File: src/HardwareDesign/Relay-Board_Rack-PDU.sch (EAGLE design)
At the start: 16 parts

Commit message: add SMPS to relay board
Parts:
- added BR1: DBLS207G, rectifier:DBLS207G
- added C14: 100nF 275V, ds_passive:C
- added C15, C17: 15uF 400V, Capacitor:C-POL_RADIAL-25MM-DIA
- added C16: 10nF 1kV, ds_passive:C-1206
- added C18: 470uF 25V, Capacitor:C-POL_RADIAL-11MM-DIA
- added C19, C25: 100uF 25V, Capacitor:C-POL_RADIAL-11MM-DIA
- added C20: 1uF 25V, ds_passive:C-0805
- added C21: 10nF 50V, ds_passive:C-0805
- added C22: 2.2nF 50V, ds_passive:C-0603
- added C23: 33nF 16V, ds_passive:C-0603
- added C24: 220pF, ds_passive:C-0805
- added C26: DE2E3KY222MA2BM01, ds_passive:C102-1KV
- added CM1: 20mH CM CHOKE, ds_trafo:WE-CMB_XS_744821120
- added CON1: (no value), ds_con:CON-2X7
- added D15: MRA4007T3G, Diodes:SS12
- added D16: STPS5H100B, ds_active:STPS5H100B
- added D17, D18, D19: BAT41ZFILM, diode:CGRM4001-G
- added D20: MMSZ5248B-V-GS08, Diodes-2:BZG03C240-HM3-08
- added F2: 696101000002, Wurth_Connectors_WR-FSH:696101000002
- added IC3: TS432ILT, ds_ic_vreg:TS432ILT
- added IC4: (no value), ds_ic_peripherals:VIPER35HD
- added L2: 3.3uH SD43-332ML, 52101-101-REV-A_v16:INDUCTOR-BOURNS_SRN8040
- added OPT2: SFH6106-2T, ds_ic_peripherals:SFH6106-3SMD-4_SFH610X_VIS-M
- added R13: 220K 5% 0.33W 200V, ds_passive:R1206
- added R14: 1K, ds_passive:R0603
- added R15: 12K, ds_passive:R0603
- added R16: 82K, ds_passive:R0603
- added R17: 130K 1%, ds_passive:R0603
- added R18: 15K 1%, ds_passive:R0603
- added R19: 4.7R 1%, ds_passive:R0603
- added R20: 330K 1%, ds_passive:R0603
- added R21: 133K 1%, ds_passive:R0603
- added R22: 30K 1%, ds_passive:R0603
- added R23: 47K 1%, ds_passive:R0603
- added R24: 220R, ds_passive:R0805
- added RV1: B72210S0321K101, varistor:S10K40
- added T1: 750370228, ds_trafo:750370228
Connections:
- new net AC_LINE2: C14.2, CM1.1, RV1.2
- new net AGND: BR1.-, C15.-, C17.-, C22.2, C24.2, C25.-, C26.1, D17.A, D20.A, IC4.BR, IC4.GND, OPT2.4, R22.2, R23.2, T1.3
- new net DC_RAW: BR1.+, C15.+, C16.1, C17.+, R13.2, T1.6
- new net FB: C22.1, C23.1, IC4.FB, OPT2.3
- new net GND: C18.-, C19.-, C20.2, C26.2, IC3.3, R18.2, T1.10
- new net N$12: BR1.AC2, CM1.3
- new net N$20: C14.1, CM1.2, F2.2, RV1.1
- new net N$22: C16.2, D15.C, R13.1
- new net N$23: D15.A, IC4.DRAIN, T1.4
- new net N$24: D16.2, T1.8
- new net N$25: C18.+, D16.3, L2.1, R14.1
- new net N$26: IC3.2, OPT2.1, R14.2, R15.1
- new net N$27: OPT2.2, R15.2, R16.1
- new net N$28: C21.1, R16.2
- new net N$29: C21.2, IC3.1, R17.2, R18.1
- new net N$30: C24.1, C25.+, D19.C, IC4.VDD, R24.1
- new net N$31: D19.A, R19.2
- new net N$32: D18.A, R19.1, R20.1, T1.1
- new net N$33: D17.C, D18.C, R21.1
- new net N$34: IC4.ZCD, R20.2, R21.2, R22.1
- new net N$35: C23.2, R23.1
- new net N$36: D20.C, R24.2
- new net N$5: BR1.AC1, CM1.4
- net +12V: now also C19.+, C20.1, L2.2, R17.1
- net AC_LINE: now also F2.1
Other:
- note added: "12 V - 15 W FLYBACK CONVERTER"

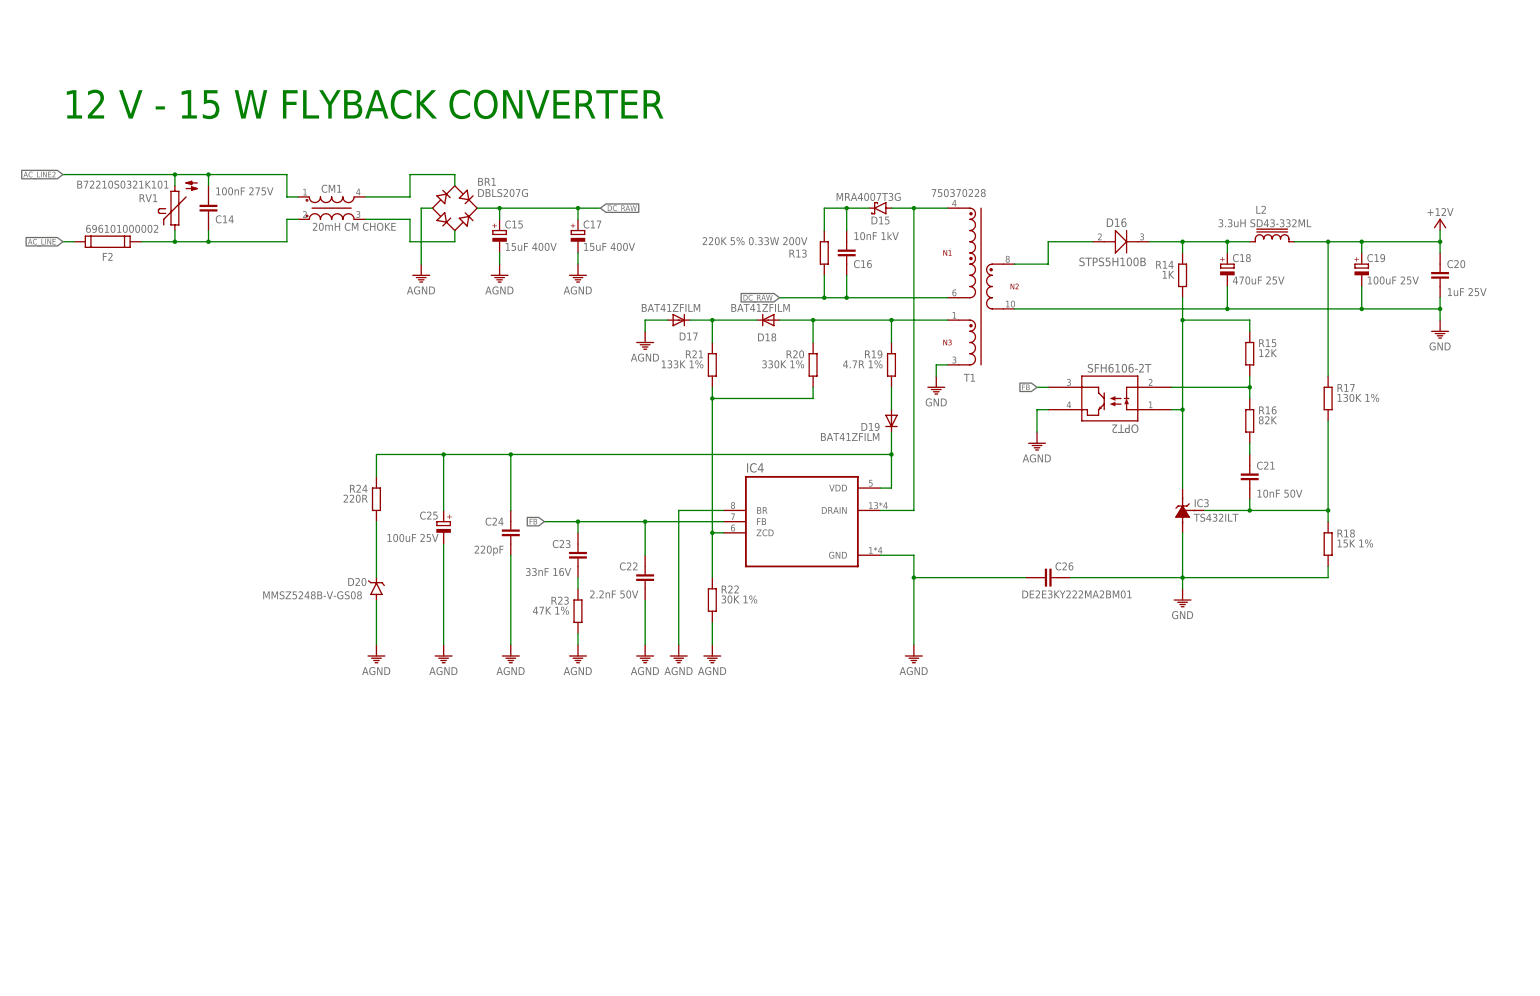
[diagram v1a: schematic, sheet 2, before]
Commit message: finish relay board design
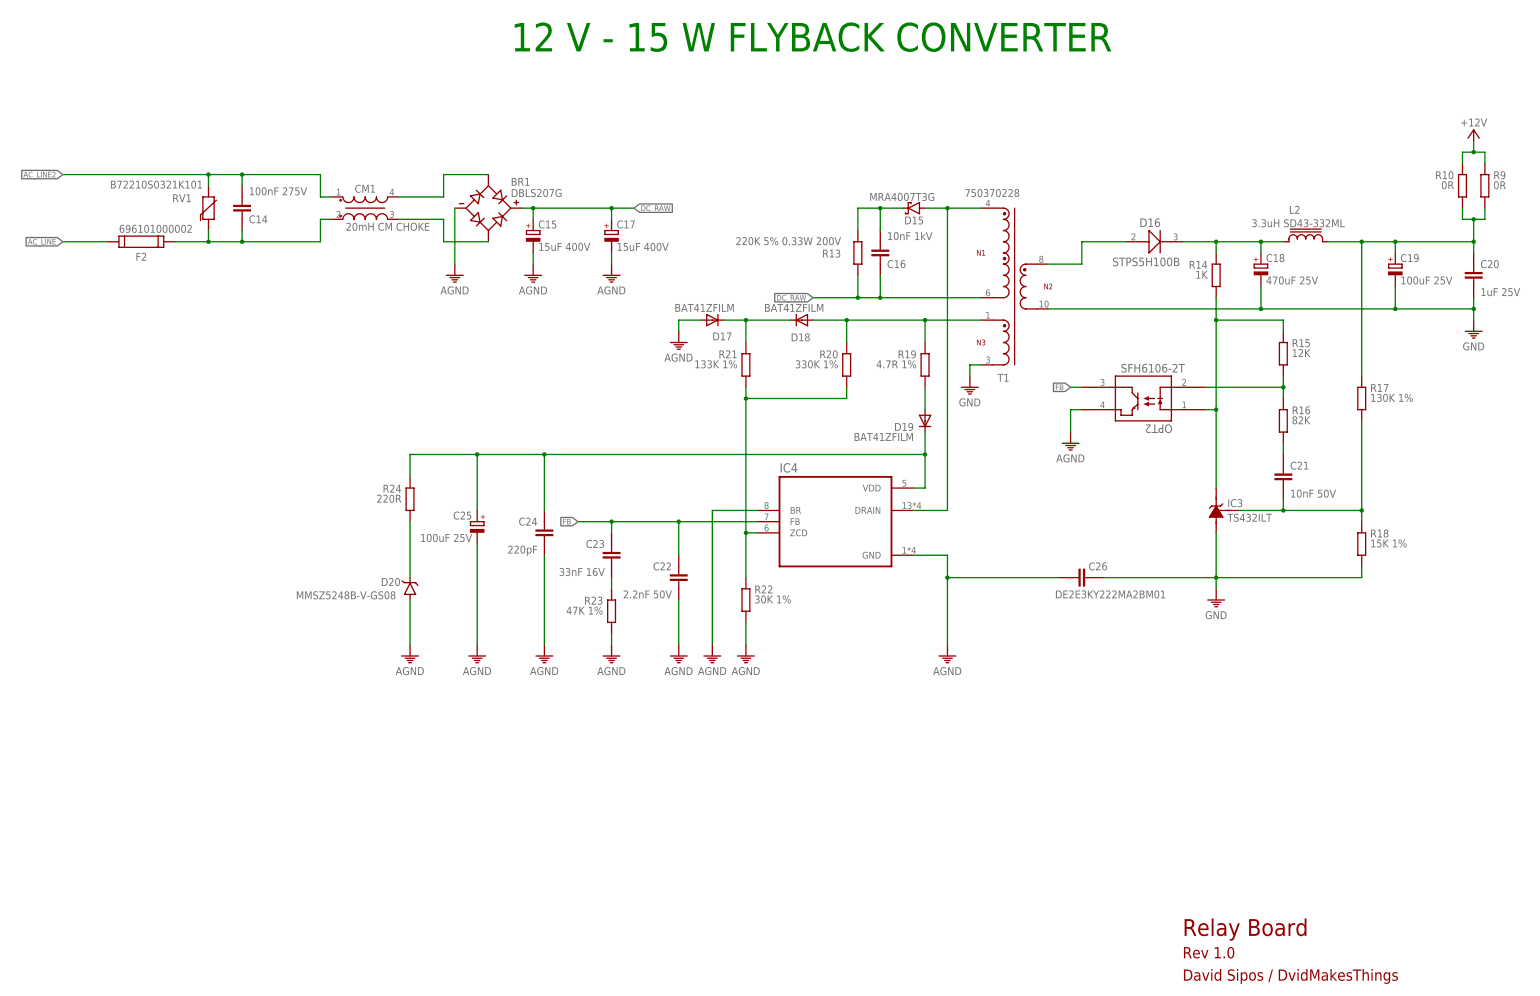
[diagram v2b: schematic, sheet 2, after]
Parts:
- added IC1: ULN2803, ds_ic_peripherals:ULN2803
- added R1, R2, R3, R4, R5, R6, R7, R8: 330R 1W, ds_passive:R1206
- added R10, R9: 0R, ds_passive:R0805
- BR1: device rectifier:DBLS207G -> ds_active:DBLS207G
- RV1: device varistor:S10K40 -> Wurth_EMC Components_WE-VD:WE-VD_10MM_820412001
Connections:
- new net +3V3: CON1.1
- new net +5V: CON1.2
- new net I_MEA/TX: CON1.4
- new net N$10: IC1.5C, R5.1
- new net N$11: IC1.6C, R6.1
- new net N$13: IC1.7C, R7.1
- new net N$15: IC1.8C, R8.1
- new net N$2: C19.+, C20.1, L2.2, R10.2, R17.1, R9.2
- new net N$6: IC1.1C, R1.1
- new net N$7: IC1.2C, R2.1
- new net N$8: IC1.3C, R3.1
- new net N$9: IC1.4C, R4.1
- new net REL_0: CON1.12, IC1.1B
- new net REL_1: CON1.11, IC1.2B
- new net REL_2: CON1.10, IC1.3B
- new net REL_3: CON1.9, IC1.4B
- new net REL_4: CON1.8, IC1.5B
- new net REL_5: CON1.7, IC1.6B
- new net REL_6: CON1.6, IC1.7B
- new net REL_7: CON1.5, IC1.8B
- new net VMEA/RX: CON1.3
- net +12V: now also CON1.14, IC1.COM, R10.1, R9.1; no longer C19.+, C20.1, L2.2, R17.1
- net GND: now also CON1.13, IC1.GND
- net RELAY_1: now also R1.2
- net RELAY_2: now also R2.2
- net RELAY_3: now also R3.2
- net RELAY_4: now also R4.2
- net RELAY_5: now also R5.2
- net RELAY_6: now also R6.2
- net RELAY_7: now also R7.2
- net RELAY_8: now also R8.2
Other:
- note added: "DRIVER CONNECTOR"
- note added: "David Sipos / DvidMakesThings"
- note added: "Relay Board"
- note added: "Rev 1.0"
- note added: "ULN2803 RELAY DRIVER"
- moved on the sheet: C14, C15, C16, C17, C18, C19, C20, C21, C22, C23, C24, C25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

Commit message: first order send to JLCPCB
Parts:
- C14: value 100nF 275V -> MP2104K27C3R6LC 100nF 275V
- C15, C17: value 15uF 400V -> KM150M400G160A 15uF 400V
- D1: value MBRA340T3 -> MBRA340T3G
- IC1: value ULN2803 -> ULN2803A
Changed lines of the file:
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@@
 <part name="FRAME1" library="frames" library_urn="urn:adsk.eagle:library:229" deviceset="A3L-LOC" device=""/>
 <part name="REL1" library="ds_passive" deviceset="G2RL-1A-E_DC12" device="" package3d_urn="urn:adsk.eagle:package:46756717/2"/>
-<part name="D1" library="diode" library_urn="urn:adsk.eagle:library:210" deviceset="MBRA340T3" device="" package3d_urn="urn:adsk.eagle:package:43460/3"/>
+<part name="D1" library="diode" library_urn="urn:adsk.eagle:library:210" deviceset="MBRA340T3" device="" package3d_urn="urn:adsk.eagle:package:43460/3" value="MBRA340T3G"/>
 <part name="P+1" library="ds_passive" deviceset="+12V" device=""/>
 <part name="REL2" library="ds_passive" deviceset="G2RL-1A-E_DC12" device="" package3d_urn="urn:adsk.eagle:package:46756717/2"/>
@@
 <part name="BR1" library="ds_active" deviceset="DBLS207G" device="" package3d_urn="urn:adsk.eagle:package:46780836/2" value="DBLS207G"/>
 <part name="RV1" library="Wurth_EMC Components_WE-VD" library_urn="urn:adsk.eagle:library:14283070" deviceset="WE-VD_10MM" device="_820412001" package3d_urn="urn:adsk.eagle:package:12144824/3" value="B72210S0321K101"/>
-<part name="C14" library="ds_passive" deviceset="C" device="" package3d_urn="urn:adsk.eagle:package:46766481/2" value="100nF 275V"/>
+<part name="C14" library="ds_passive" deviceset="C" device="" package3d_urn="urn:adsk.eagle:package:46766481/2" value="MP2104K27C3R6LC 100nF 275V"/>
 <part name="F2" library="Wurth_Connectors_WR-FSH" library_urn="urn:adsk.eagle:library:14787550" deviceset="696101000002" device="" package3d_urn="urn:adsk.eagle:package:14787579/2" value="696101000002"/>
 <part name="GND6" library="ds_passive" deviceset="AGND" device=""/>
 <part name="GND7" library="ds_passive" deviceset="AGND" device=""/>
-<part name="C15" library="Capacitor" library_urn="urn:adsk.eagle:library:16290819" deviceset="C-POL" device="RADIAL-25MM-DIA" package3d_urn="urn:adsk.eagle:package:16290890/3" technology="_" value="15uF 400V"/>
+<part name="C15" library="Capacitor" library_urn="urn:adsk.eagle:library:16290819" deviceset="C-POL" device="RADIAL-25MM-DIA" package3d_urn="urn:adsk.eagle:package:16290890/3" technology="_" value="KM150M400G160A 15uF 400V"/>
 <part name="FRAME3" library="frames" library_urn="urn:adsk.eagle:library:229" deviceset="A3L-LOC" device=""/>
 <part name="R13" library="ds_passive" deviceset="R" device="1206" package3d_urn="urn:adsk.eagle:package:46683745/2" value="220K 5% 0.33W 200V"/>
 <part name="C16" library="ds_passive" deviceset="C" device="-1206" package3d_urn="urn:adsk.eagle:package:46766482/2" value="10nF 1kV"/>
 <part name="CM1" library="ds_trafo" deviceset="WE-CMB_XS_744821120" device="" package3d_urn="urn:adsk.eagle:package:46769279/2" value="20mH CM CHOKE"/>
-<part name="C17" library="Capacitor" library_urn="urn:adsk.eagle:library:16290819" deviceset="C-POL" device="RADIAL-25MM-DIA" package3d_urn="urn:adsk.eagle:package:16290890/3" technology="_" value="15uF 400V"/>
+<part name="C17" library="Capacitor" library_urn="urn:adsk.eagle:library:16290819" deviceset="C-POL" device="RADIAL-25MM-DIA" package3d_urn="urn:adsk.eagle:package:16290890/3" technology="_" value="KM150M400G160A 15uF 400V"/>
 <part name="GND9" library="ds_passive" deviceset="AGND" device=""/>
 <part name="D15" library="Diodes" library_urn="urn:adsk.eagle:library:11396254" deviceset="SS12" device="" package3d_urn="urn:adsk.eagle:package:10898394/2" value="MRA4007T3G"/>
@@
 <part name="R6" library="ds_passive" deviceset="R" device="1206" package3d_urn="urn:adsk.eagle:package:46683745/2" value="330R 1W"/>
 <part name="R7" library="ds_passive" deviceset="R" device="1206" package3d_urn="urn:adsk.eagle:package:46683745/2" value="330R 1W"/>
-<part name="IC1" library="ds_ic_peripherals" deviceset="ULN2803" device="" package3d_urn="urn:adsk.eagle:package:46683893/2"/>
+<part name="IC1" library="ds_ic_peripherals" deviceset="ULN2803" device="" package3d_urn="urn:adsk.eagle:package:46683893/2" value="ULN2803A"/>
 <part name="R8" library="ds_passive" deviceset="R" device="1206" package3d_urn="urn:adsk.eagle:package:46683745/2" value="330R 1W"/>
 <part name="R9" library="ds_passive" deviceset="R" device="0805" package3d_urn="urn:adsk.eagle:package:46683742/2" value="0R"/>
@@
 <instance part="C14" gate="G$1" x="76.2" y="182.88" smashed="yes" rot="MR180">
 <attribute name="NAME" x="77.724" y="181.229" size="1.778" layer="95" rot="MR180"/>
-<attribute name="VALUE" x="77.724" y="187.579" size="1.778" layer="96" rot="MR180"/>
+<attribute name="VALUE" x="70.104" y="192.659" size="1.778" layer="96" rot="MR180"/>
 </instance>
 <instance part="F2" gate="G$1" x="53.34" y="175.26" smashed="yes" rot="MR180">
@@
 <instance part="C15" gate="G$1" x="142.24" y="177.8" smashed="yes">
 <attribute name="NAME" x="143.383" y="178.2826" size="1.778" layer="95"/>
-<attribute name="VALUE" x="143.383" y="173.2026" size="1.778" layer="96"/>
+<attribute name="VALUE" x="143.383" y="170.6626" size="1.778" layer="96"/>
 </instance>
 <instance part="FRAME3" gate="G$1" x="0" y="0" smashed="yes">
@@
 <instance part="R13" gate="G$1" x="215.9" y="172.72" smashed="yes" rot="MR0">
 <attribute name="NAME" x="212.09" y="171.6786" size="1.778" layer="95" rot="MR0"/>
-<attribute name="VALUE" x="212.09" y="174.498" size="1.778" layer="96" rot="MR0"/>
+<attribute name="VALUE" x="212.09" y="177.038" size="1.778" layer="96" rot="MR0"/>
 </instance>
 <instance part="C16" gate="G$1" x="220.98" y="172.72" smashed="yes" rot="MR180">

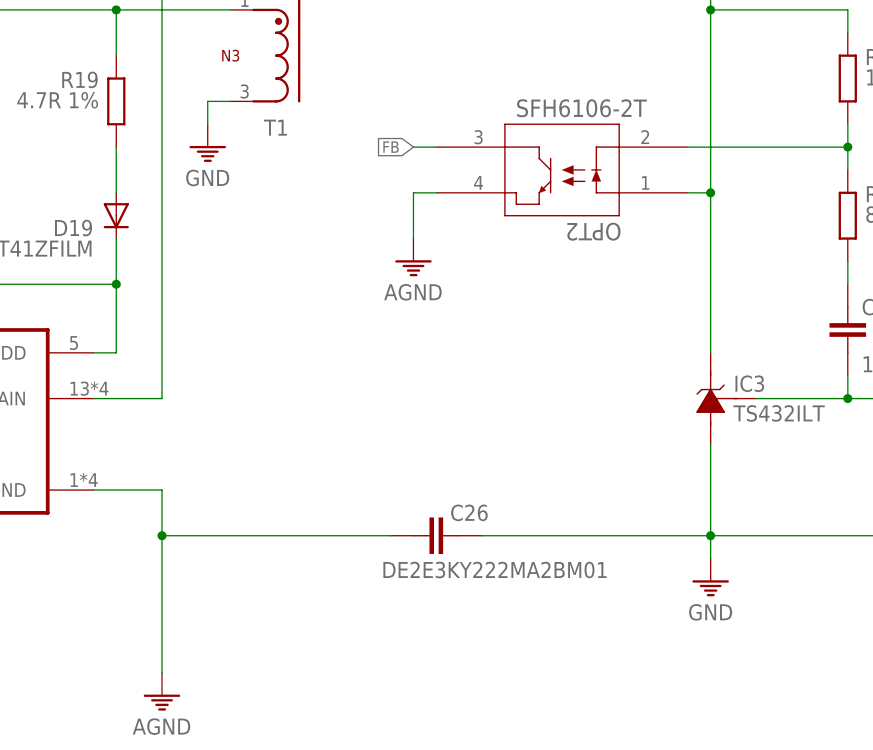
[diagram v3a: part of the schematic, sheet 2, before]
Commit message: change X1, X2 because of shortage
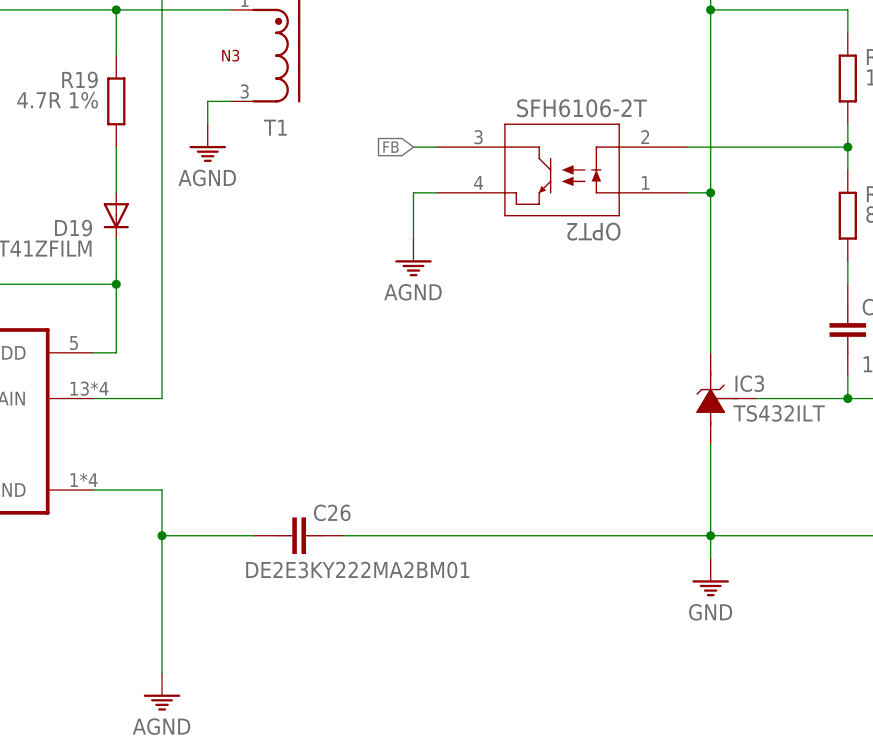
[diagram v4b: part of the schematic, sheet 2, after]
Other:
- moved on the sheet: C26
